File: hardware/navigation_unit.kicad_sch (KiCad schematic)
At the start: 34 parts, among them SW1 SW_Push_Dual, SW2 SW_SPDT_312, SW3 SW_SPDT_312, U1 STM32F405RGTx, Y1 25MHz

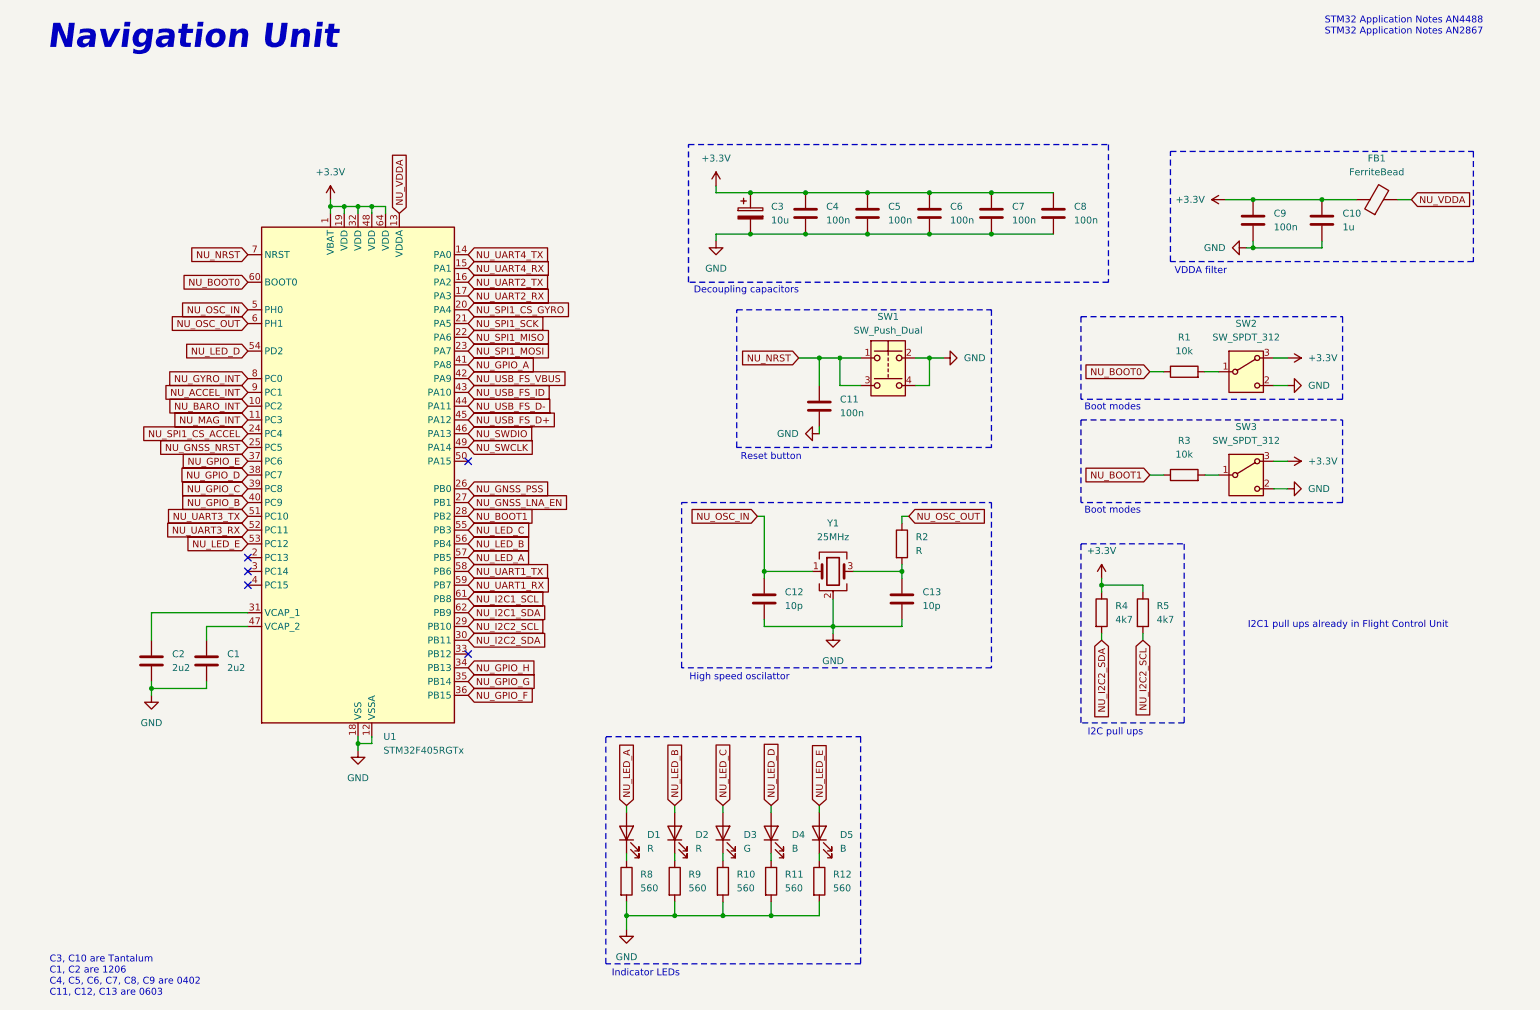
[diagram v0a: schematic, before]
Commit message: schematic and BOM done
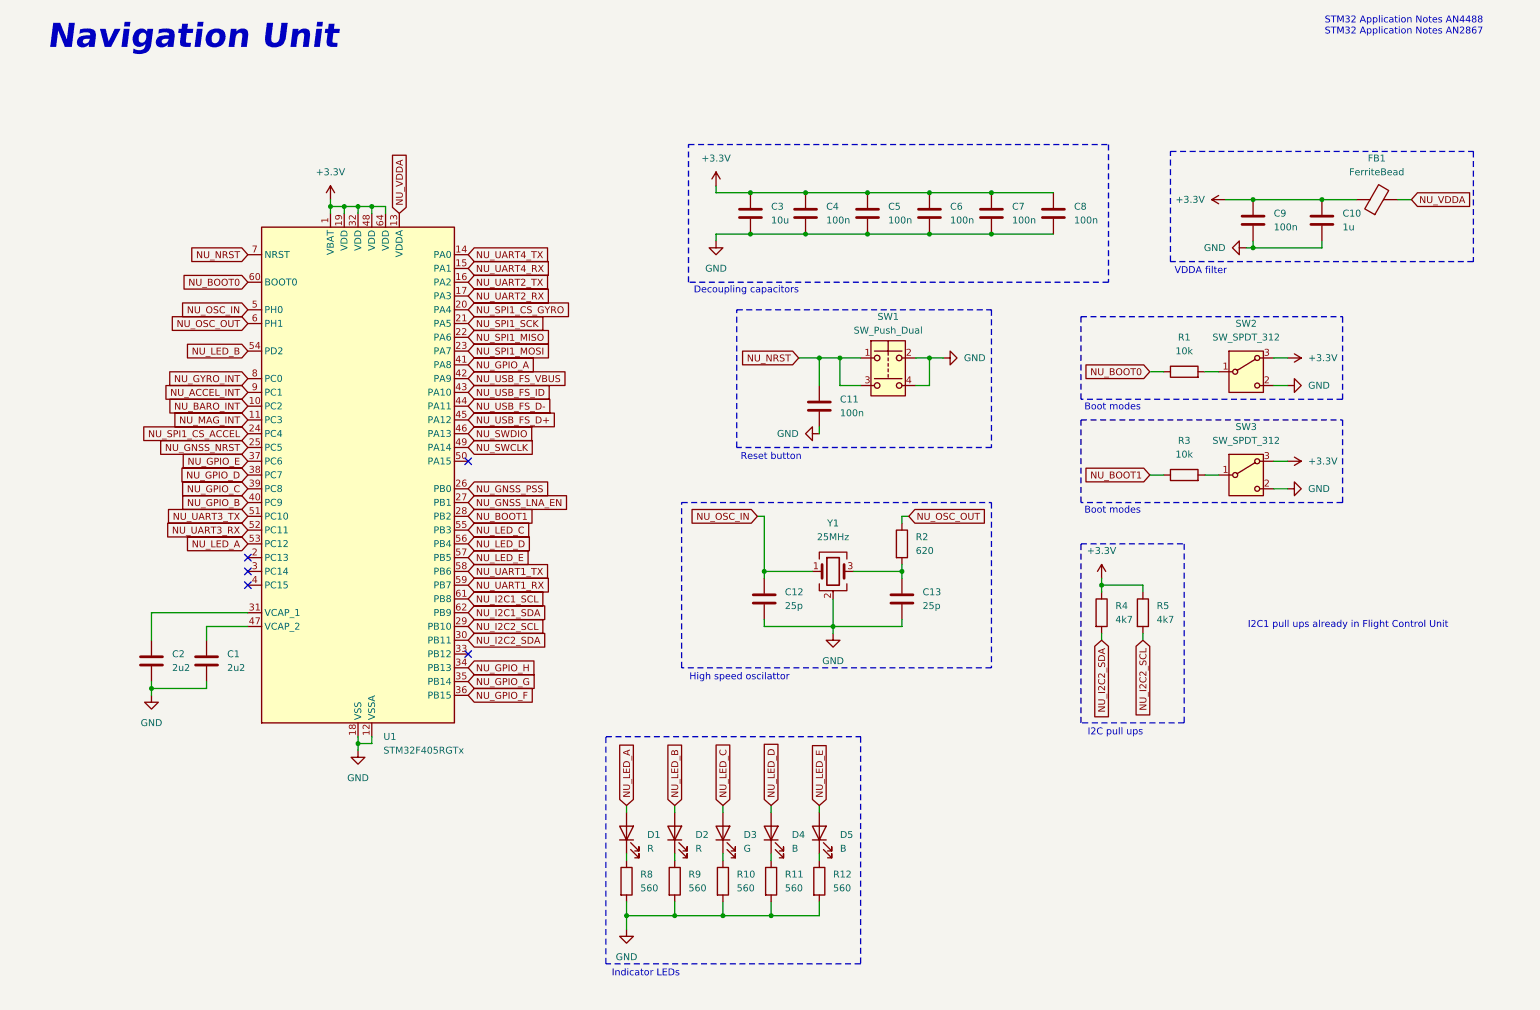
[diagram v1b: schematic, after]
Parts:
- removed C3: 10u, symbol Device:C_Polarized
- added C3: 10u, Capacitor_SMD:C_0603_1608Metric, symbol Device:C
- C1, C2: footprint (none) -> Capacitor_SMD:C_0805_2012Metric
- C10: footprint (none) -> Capacitor_SMD:C_0603_1608Metric
- C11, C4, C5, C6, C7, C8, C9: footprint (none) -> Capacitor_SMD:C_0402_1005Metric
- C12, C13: value 10p -> 25p; footprint (none) -> Capacitor_SMD:C_0603_1608Metric
- D1, D2, D3, D4, D5: footprint (none) -> LED_SMD:LED_0603_1608Metric
- FB1: footprint (none) -> Inductor_SMD:L_0603_1608Metric
- R1, R10, R11, R12, R3, R4, R5, R8, R9: footprint (none) -> Resistor_SMD:R_0603_1608Metric
- R2: value R -> 620; footprint (none) -> Resistor_SMD:R_0603_1608Metric
- SW1: footprint (none) -> airplane:SW_TL3365AF180QG; Manufacturer Part Number (none) -> TL3365AF180QG
- SW2, SW3: footprint (none) -> Button_Switch_SMD:SW_SPDT_PCM12; Manufacturer Part Number (none) -> PCM12SMTR
- U1: Manufacturer Part Number (none) -> STM32F405RGT6
- Y1: footprint (none) -> airplane:XTAL_ABM8G-25.000MHZ-18-D2Y-T; Manufacturer Part Number (none) -> ABM8G-25.000MHZ-18-D2Y-T
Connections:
- net +3.3V: now also C3.1
- net GND: now also C3.2
- net NU_LED_A: now also U1.53 (PC12); no longer U1.57 (PB5)
- net NU_LED_B: now also U1.54 (PD2); no longer U1.56 (PB4)
- net NU_LED_D: now also U1.56 (PB4); no longer U1.54 (PD2)
- net NU_LED_E: now also U1.57 (PB5); no longer U1.53 (PC12)
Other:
- note removed: "C3, C10 are Tantalum C1, C2 are 1206 C4, C5, C6, C7, C8, C9 are 0402 C11, C12, C13 are 0603"
